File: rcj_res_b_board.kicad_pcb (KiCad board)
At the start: 2 copper layers, 92.5 x 100 mm, 94 parts, among them P1 GP2Y0A41SK0F, P10 SERVO0, P11 MPU9250, P12 PING0, P13 CONN_01X03, P14 CONN_01X03, P15 CONN_01X04, P16 CONN_02X04, P2 GP2Y0A41SK0F, P3 GP2Y0A41SK0F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

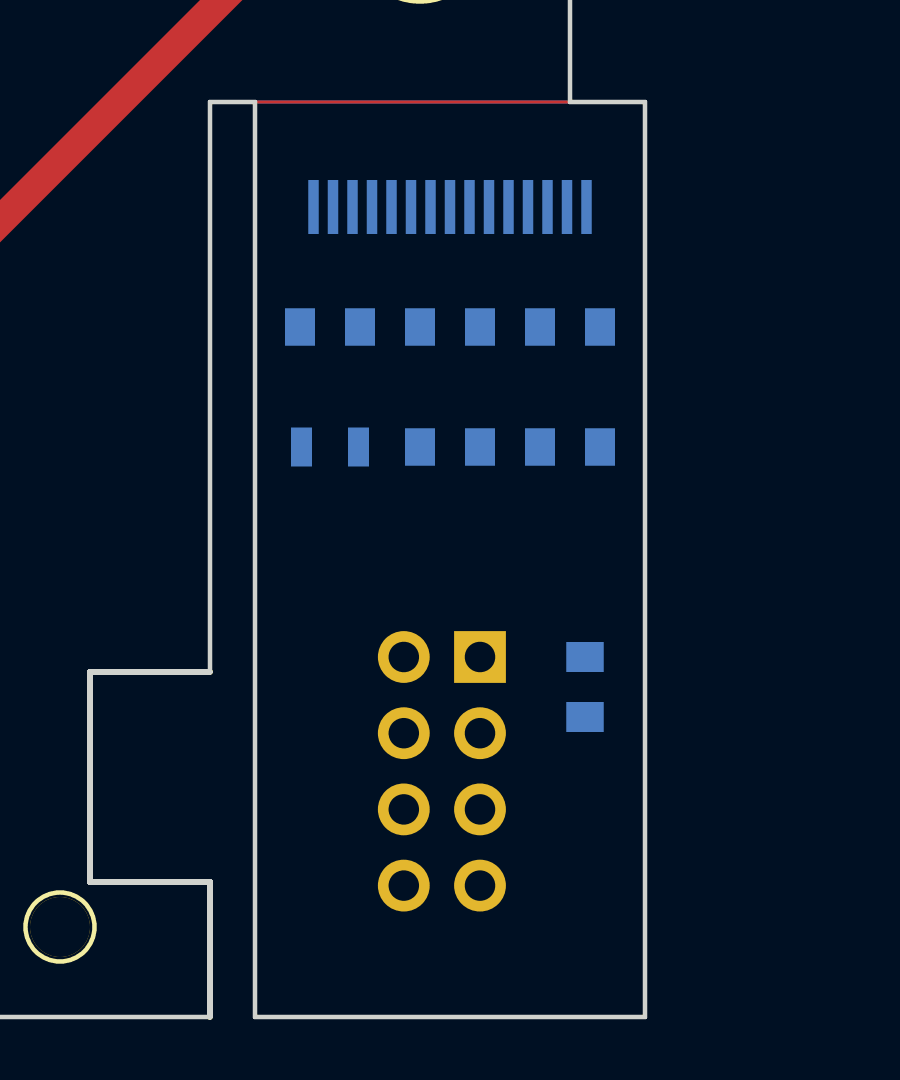
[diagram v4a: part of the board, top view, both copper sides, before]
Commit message: Flipped cutoff around
Changed copper fills to have no net
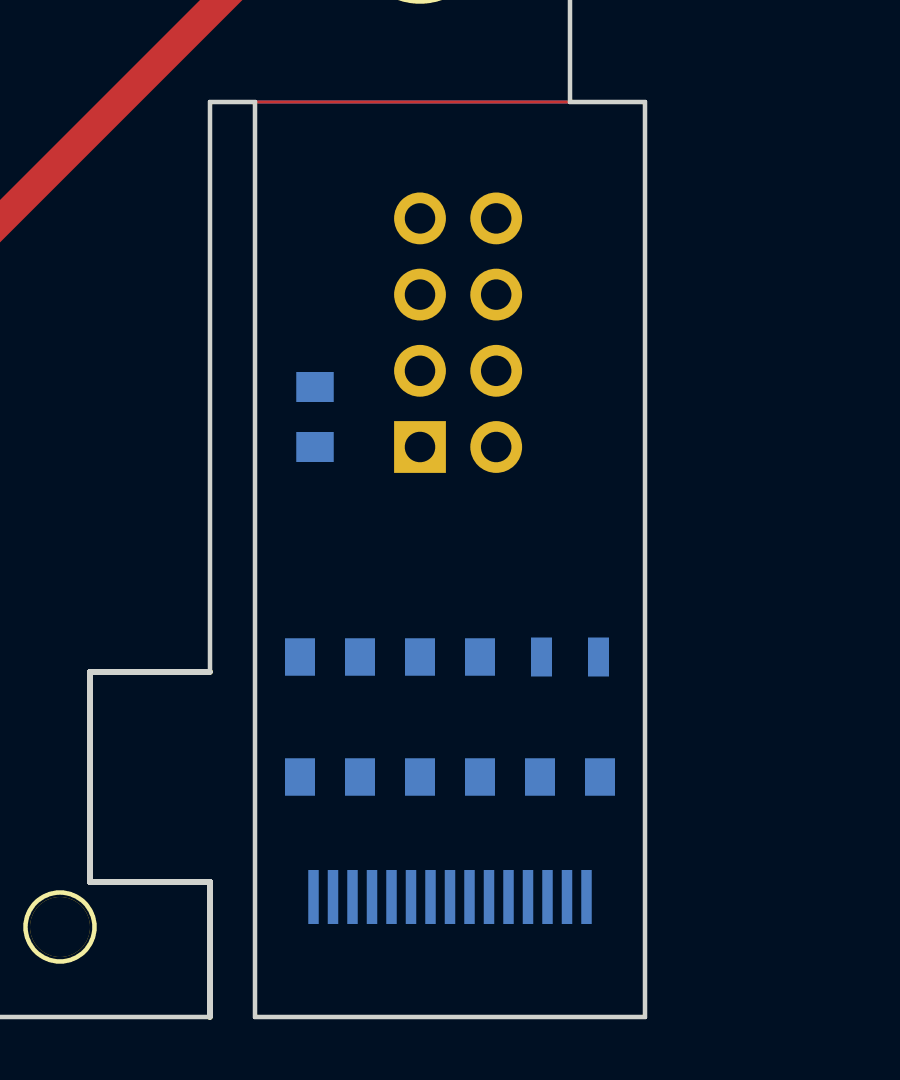
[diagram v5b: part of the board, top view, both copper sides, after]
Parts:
- moved OLED1 23.0 mm to (106.0, 146.0), turned to 90 degrees
- moved C7 17.0 mm to (102.0, 142.0), turned to 0 degrees
- moved C9 17.0 mm to (110.0, 142.0), turned to 180 degrees
- moved C8 15.0 mm to (106.0, 142.0), turned to 0 degrees
- moved C13 12.7 mm to (101.5, 130.0), turned to 270 degrees
- moved C11 10.6 mm to (102.0, 138.0), turned to 180 degrees
- moved R10 10.6 mm to (110.0, 138.0), turned to 180 degrees
- moved P_CT1 7.28 mm to (105.0, 131.0), turned to 0 degrees
- moved C12 7.00 mm to (106.0, 138.0), turned to 180 degrees

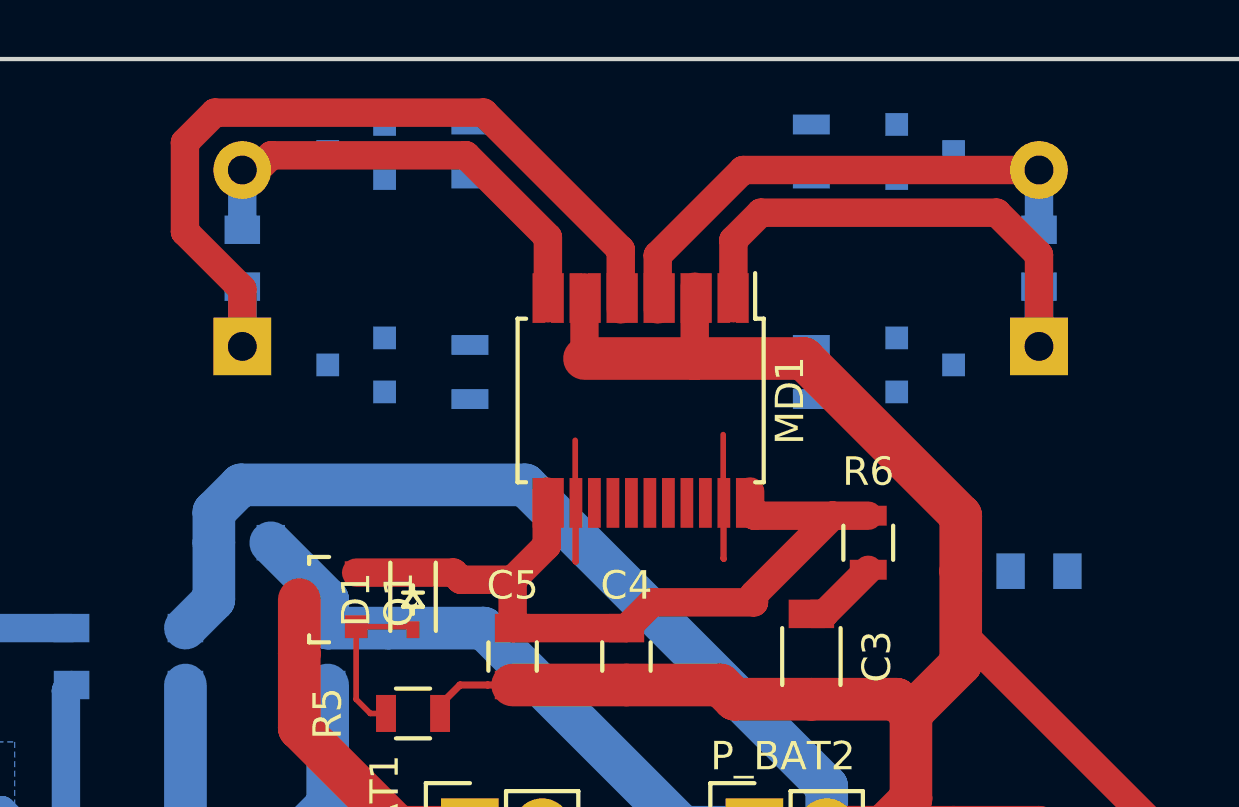
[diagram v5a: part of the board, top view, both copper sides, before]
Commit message: Moved footprints around to match physical
Hall-effect sensors and motor connectors moved towards center
Rotated one of the motor connectors
Fixed overlapping silkscreens
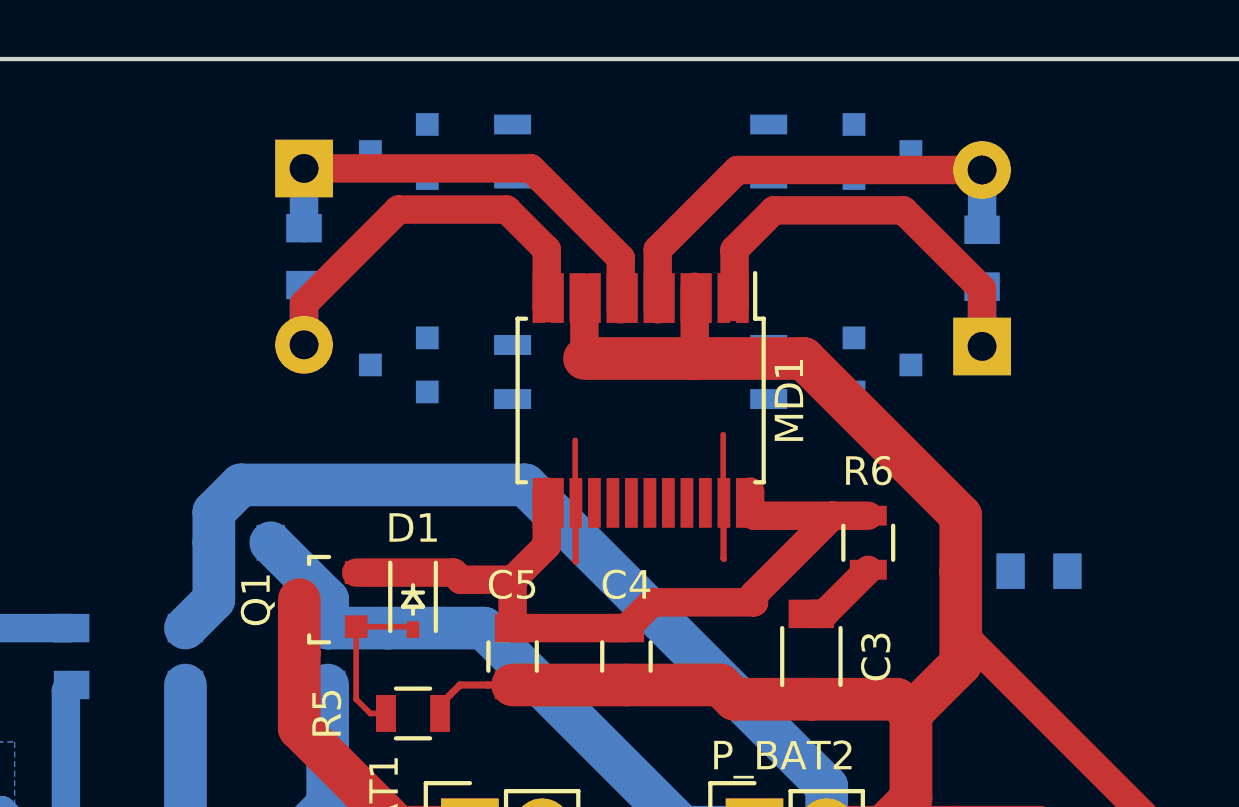
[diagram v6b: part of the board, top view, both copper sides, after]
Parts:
- moved P9 6.62 mm to (53.2, 53.8), turned to 270 degrees
- moved C2 2.17 mm to (53.2, 56.9), turned to 90 degrees
- moved C1 2.00 mm to (77.0, 57.0)
- moved P8 2.00 mm to (77.0, 60.1)
- moved HAL_M0A1 1.50 mm to (56.5, 53.2)
- moved HAL_M0B1 1.50 mm to (56.5, 60.8)
- moved HAL_M1A1 1.50 mm to (73.5, 53.2)
- moved HAL_M1B1 1.50 mm to (73.5, 60.8)
- moved R1 1.50 mm to (60.5, 53.2)
- moved R2 1.50 mm to (69.5, 53.2)
- moved R3 1.50 mm to (60.5, 61.0)
- moved R4 1.50 mm to (69.5, 61.0)
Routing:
- net Net-(C2-Pad2): track 31.0 -> 17.4 mm
- net Net-(C1-Pad1): track 20.5 -> 17.6 mm
- net Net-(C1-Pad2): track 19.7 -> 17.8 mm

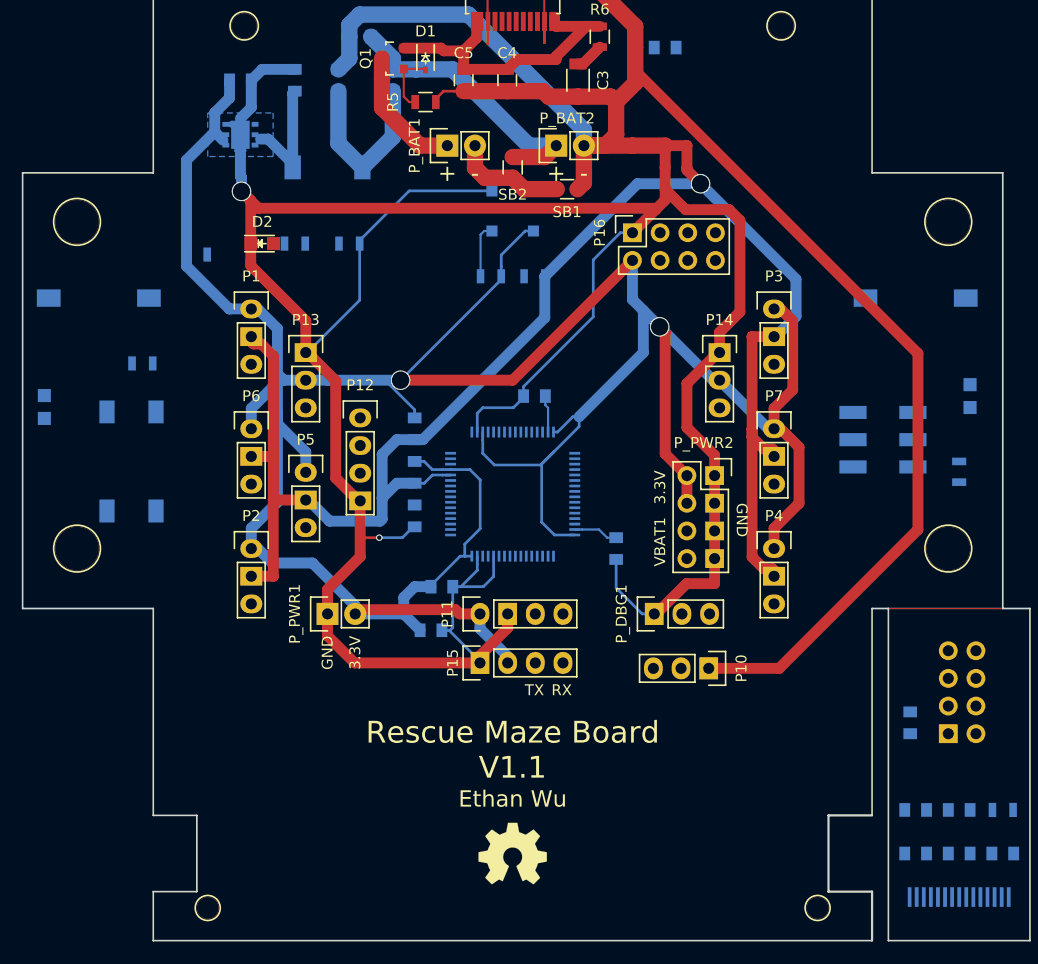
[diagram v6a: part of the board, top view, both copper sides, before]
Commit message: Re-arranged headers
Resized some screw holes
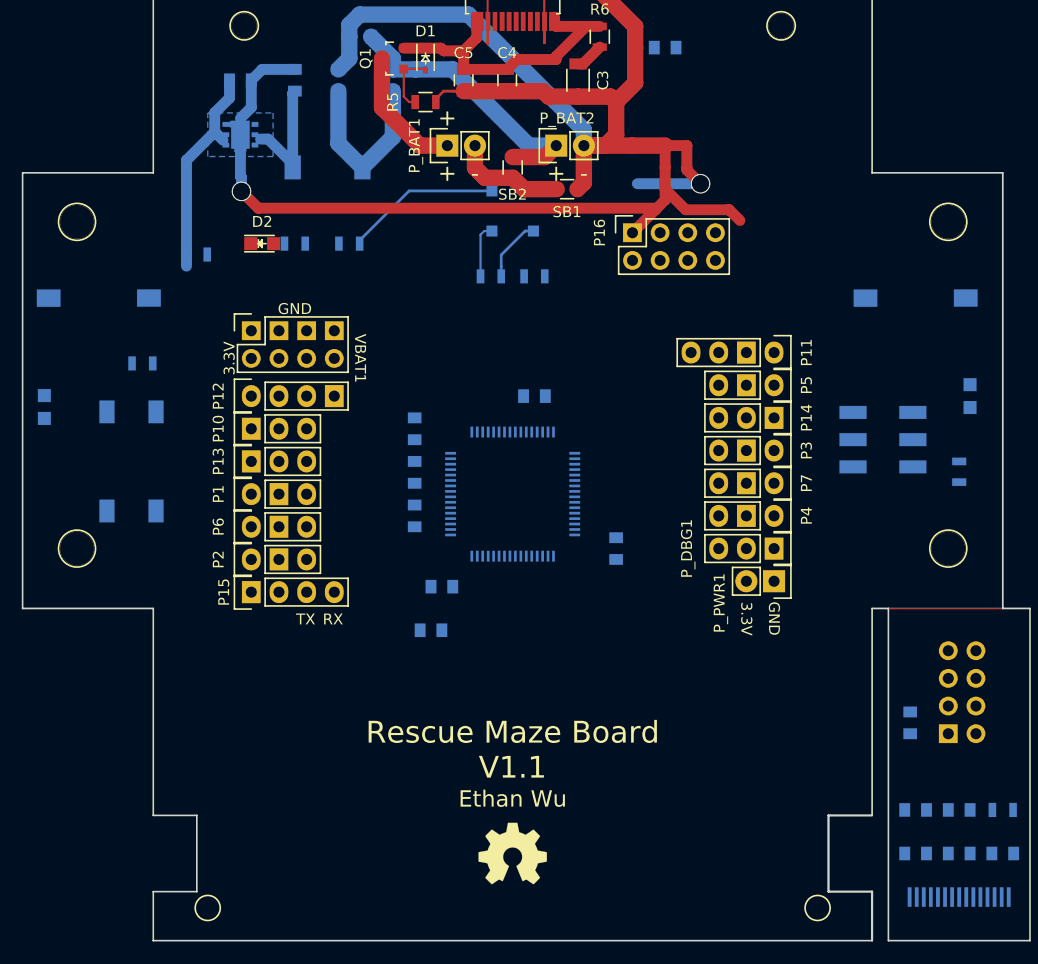
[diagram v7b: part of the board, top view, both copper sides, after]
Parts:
- moved P10 47.4 mm to (41.0, 103.0), turned to 0 degrees
- moved P_PWR2 44.6 mm to (41.0, 94.0), turned to 0 degrees
- moved P5 43.7 mm to (89.0, 99.0), turned to 180 degrees
- moved P_PWR1 41.1 mm to (89.0, 117.0), turned to 180 degrees
- moved P11 36.1 mm to (89.0, 96.0), turned to 180 degrees
- moved P15 22.0 mm to (41.0, 118.0)
- moved P1 17.0 mm to (41.0, 109.0), turned to 0 degrees
- moved P3 13.0 mm to (89.0, 105.0), turned to 180 degrees
- moved P_DBG1 12.5 mm to (89.0, 114.0), turned to 180 degrees
- moved P13 11.2 mm to (41.0, 106.0), turned to 0 degrees
- moved P12 10.2 mm to (41.0, 100.0), turned to 0 degrees
- moved P6 9.00 mm to (41.0, 112.0), turned to 0 degrees
- moved P14 7.81 mm to (89.0, 102.0), turned to 180 degrees
- moved P7 5.00 mm to (89.0, 108.0), turned to 180 degrees
- moved P4 3.00 mm to (89.0, 111.0), turned to 180 degrees
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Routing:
- net /3.3V: track 299.6 -> 26.8 mm, vias 2 -> 0
- net GNDD: track 269.4 -> 88.1 mm, vias 2 -> 1
- net GNDA: track 142.8 -> 7.82 mm
- net GNDPWR: track 127.5 -> 50.1 mm
- net Net-(C23-Pad1): track 4.11 -> 0.00 mm
- net Net-(C21-Pad1): track 3.40 -> 0.00 mm
